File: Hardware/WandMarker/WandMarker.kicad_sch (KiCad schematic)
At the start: 14 parts, among them J1 FROM DRIVER, Q1 MMBT2222A, Q2 MMBT3904

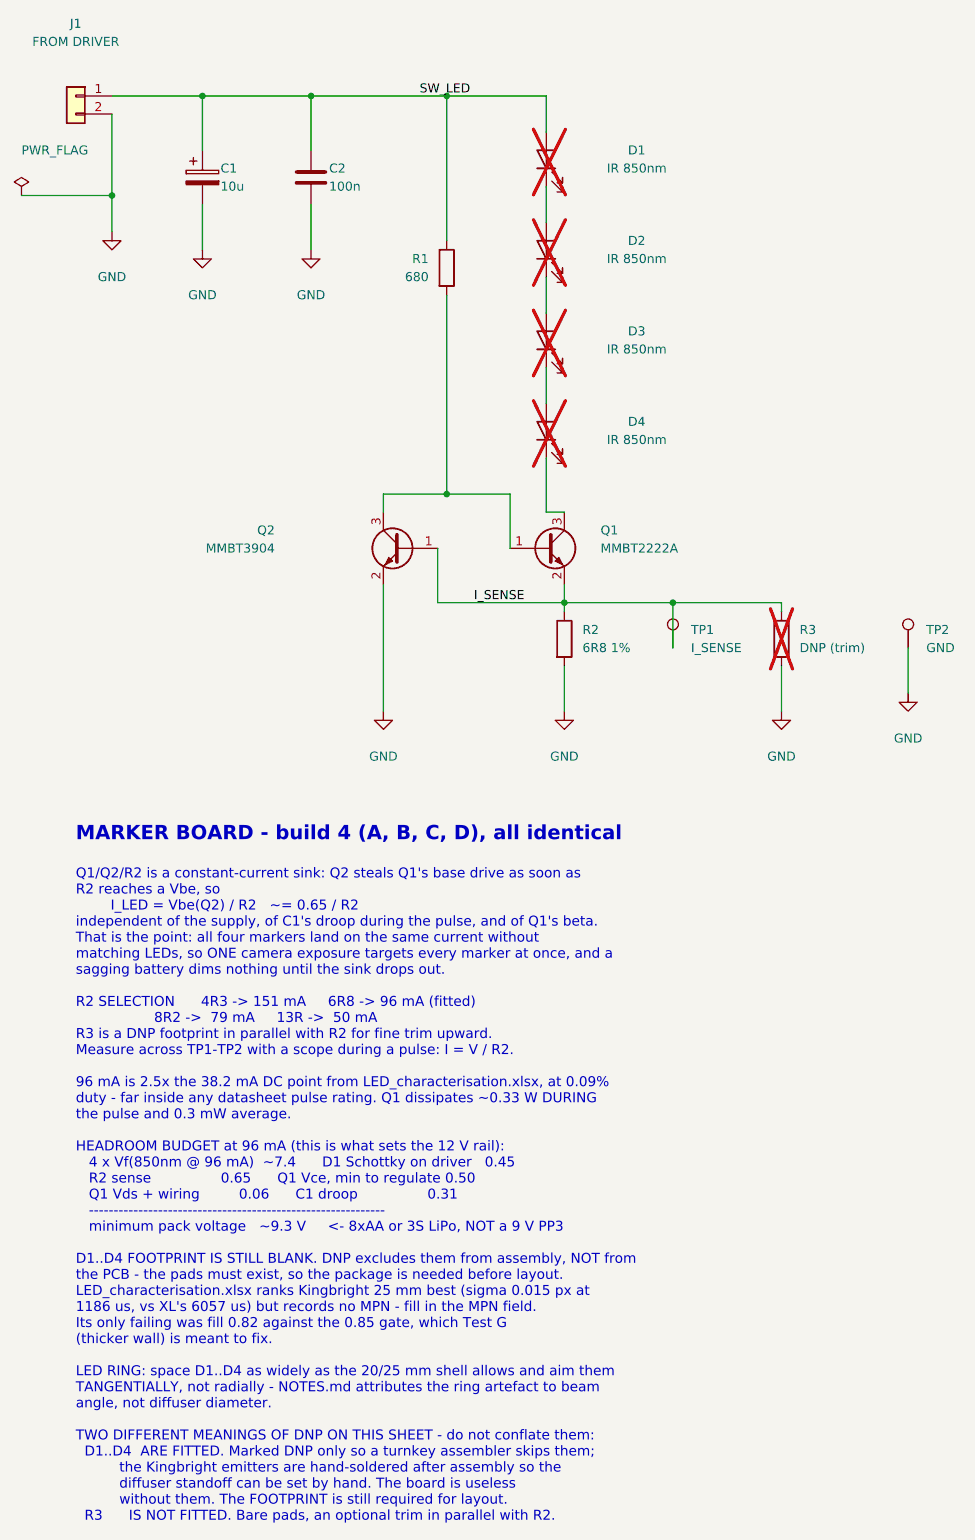
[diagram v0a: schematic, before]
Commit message: Strobe driver rev B: 9 V, fixed resistors, and the driver PCB
Rev A ran 12 V and put a constant-current sink on every marker board. The
sink cost 1.6 V of headroom - a Vbe of sense, a Vce of regulation, and the
input Schottky - and that 1.6 V was the entire reason 12 V was needed. What
it bought was marker-to-marker matching of about 5%, against ~3% run-to-run
repeatability in the characterisation itself. It was buying matching finer
than the measurement can resolve, so it is gone.

The marker board is now the board that was already characterised plus a
connector: four LEDs, one ballast resistor, eight parts. The existing bench
markers plug straight into the driver, and at 9 V they draw 36 mA - the
characterised operating point - so the strobe test is directly comparable
with the DC rows in LED_characterisation.xlsx.

Also settled from the datasheet (Kingbright L-7113SF7C, DSAB9772):

- 1.6 V is the forward drop AT 20 mA, not a constant. At 36 mA it is ~1.48 V,
  so the string is 5.9 V rather than the 6.4 V a flat 1.6 V implies. The
  workbook's 38.2 mA was computed from the 1.6 V figure; the real current
  through 68 R at 9 V is nearer 43 mA. Worth measuring, it appears in the
  thesis.
- The 1 A peak rating is quoted at a 10 us pulse, 80x shorter than ours, so
  it does not apply. What does apply is average power: 0.19 mW against an
  80 mW limit.
- The 20 degree viewing angle is the ring artefact, which is why the emitters
  must be aimed tangentially rather than radially.

No diode across R2, and none is needed. The usual sub-50% duty trick assumes
the LEDs are on when OUT is high; they are not. Q1 is P-channel on the high
side and conducts when OUT is low, so the short state is already the one we
want. Adding the diode would force R1 small and sink ~20 mA through DISCH for
the whole 327 ms off-time, against the 9 uA the circuit actually draws.

Driver PCB: 80 x 60 mm, two layers, 0 DRC violations, 0 unconnected pads.
B.Cu is the ground return; only the gate esc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
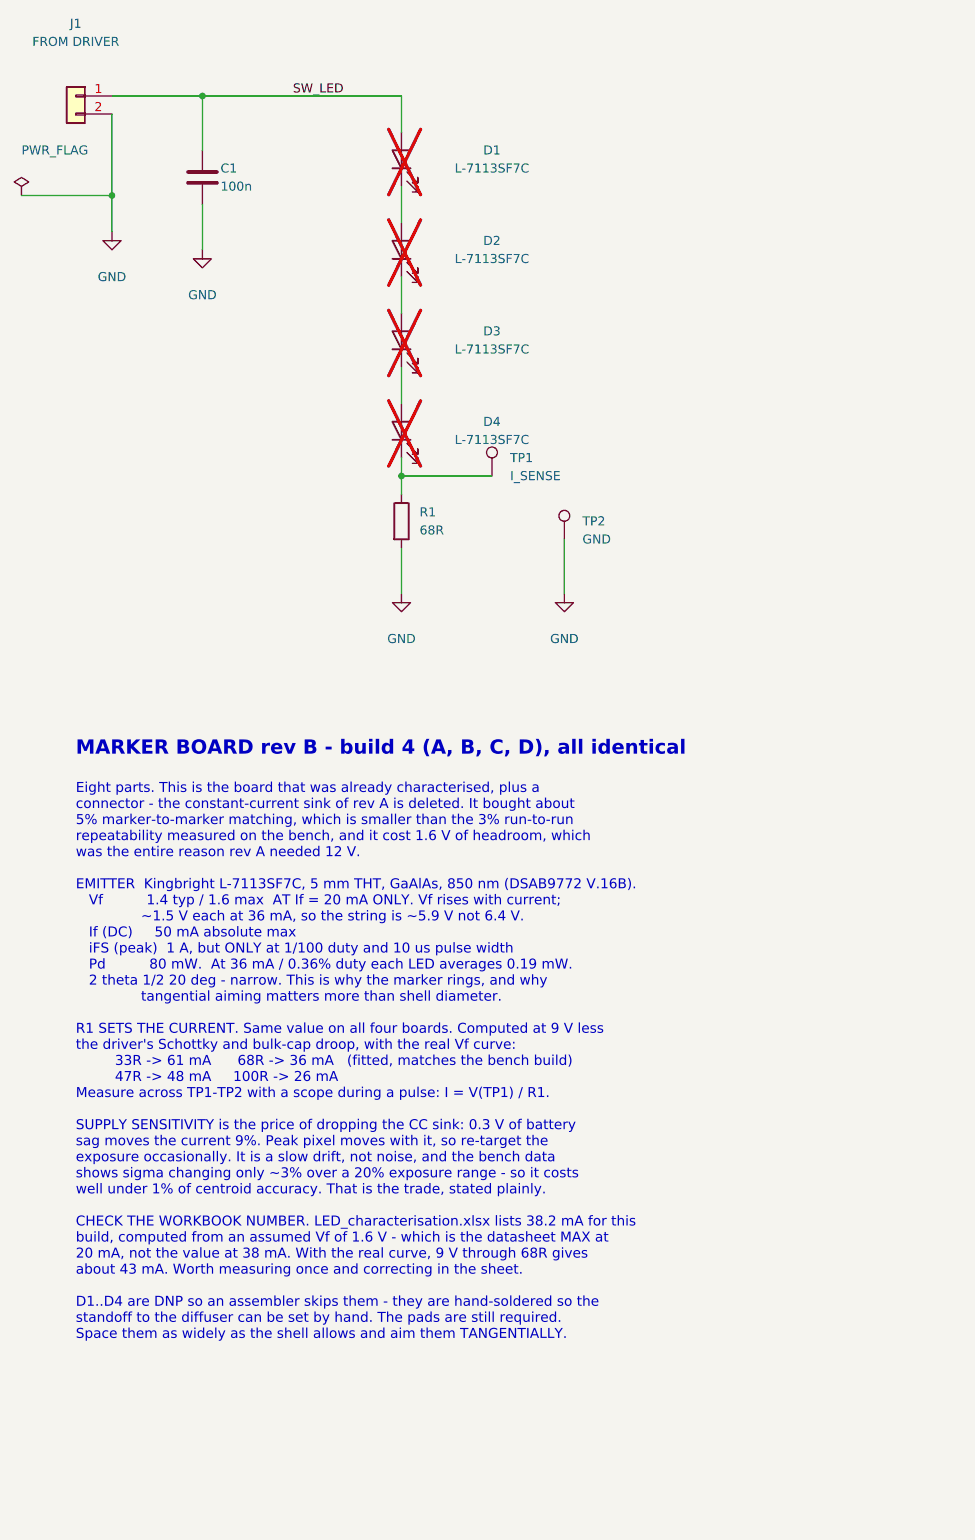
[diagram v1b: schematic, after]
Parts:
- removed C2: 100n, Capacitor_SMD:C_0805_2012Metric, symbol Device:C
- removed Q1: MMBT2222A, Package_TO_SOT_SMD:SOT-23, symbol Transistor_BJT:Q_NPN_BEC
- removed Q2: MMBT3904, Package_TO_SOT_SMD:SOT-23, symbol Transistor_BJT:Q_NPN_BEC
- removed R2: 6R8 1%, Resistor_SMD:R_1206_3216Metric, symbol Device:R
- removed R3: DNP (trim), Resistor_SMD:R_1206_3216Metric, symbol Device:R
- C1: value 10u -> 100n; footprint Capacitor_THT:CP_Radial_D5.0mm_P2.00mm -> Capacitor_SMD:C_0805_2012Metric; symbol Device:C_Polarized -> Device:C
- D1, D2, D3, D4: value IR 850nm -> L-7113SF7C; footprint (none) -> LED_THT:LED_D5.0mm; MPN Kingbright 850 nm - fill in exact MPN -> Kingbright L-7113SF7C
- R1: value 680 -> 68R; footprint Resistor_SMD:R_0805_2012Metric -> Resistor_THT:R_Axial_DIN0207_L6.3mm_D2.5mm_P10.16mm_Horizontal
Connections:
- net I_SENSE is gone; now on an unnamed net: TP1.1
- net GND: now also R1.2
- net SW_LED: no longer R1.1
- net at D4.1 (K): now also R1.1
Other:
- note added: "Eight parts. This is the board that was already characterised, plus a connector - the constant-current sink of rev A is deleted. It bought about 5% marker-to-marker matching, which is smaller than the 3% run-to-run repeatability measured on the bench, and it cost 1.6 V of headroom, which was the entire reason rev A needed 12 V. EMITTER Kingbright L-7113SF7C, 5 mm THT, GaAlAs, 850 nm (DSAB9772 V.1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"
- note added: "MARKER BOARD rev B - build 4 (A, B, C, D), all identical"
- note removed: "MARKER BOARD - build 4 (A, B, C, D), all identical"
- note removed: "Q1/Q2/R2 is a constant-current sink: Q2 steals Q1's base drive as soon as R2 reaches a Vbe, so I_LED = Vbe(Q2) / R2 ~= 0.65 / R2 independent of the supply, of C1's droop during the pulse, and of Q1's beta. That is the point: all four markers land on the same current without matching LEDs, so ONE camera exposure targets every marker at once, and a sagging battery dims nothing until the sink drops 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"
- title: Wand marker - 4x 850 nm IR LED + constant-current sink -> Wand marker - 4x Kingbright L-7113SF7C + one ballast resistor
